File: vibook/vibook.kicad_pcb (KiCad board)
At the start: 2 copper layers, 15 x 89.5 mm, 53 parts, among them IC3 STLQ020C33R, J1 Conn_ARM_JTAG_SWD_10, SW3 SW_Push, U2 STM32L011K4Ux, U3 MPR121QR2, U5 MPR121QR2

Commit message: updated board design
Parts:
- removed U1, U4: ~, jlc:12matrix
- added C12: 470u, Capacitor_Tantalum_SMD:CP_EIA-7360-38_Kemet-E, F.Cu at (102.6, 111.5)
- added J2: 6861XX148922_686112148922, 6861XX148922_686112148922:686112148922, F.Cu at (51.0, 107.5)
- added J3: 6861XX148922_686112148922, 6861XX148922_686112148922:686112148922, F.Cu at (31.5, 107.5)
- U6: value ~ -> DFR0299; footprint jlc:2pin -> DFR0299:MODULE_DFR0299
- U7: footprint jlc:2pin -> Connector_Molex:Molex_PicoBlade_53047-0210_1x02_P1.25mm_Vertical
- U9: footprint jlc:2pin -> Connector_PinHeader_2.54mm:PinHeader_1x02_P2.54mm_Horizontal
- moved R2 112.7 mm to (25.0, 96.8), turned to -90 degrees
- moved C11 111.5 mm to (27.5, 95.3), turned to 180 degrees
- moved R19 109.3 mm to (23.5, 101.5), turned to -90 degrees
- moved R20 107.7 mm to (25.0, 101.5), turned to -90 degrees
- moved R21 106.0 mm to (26.5, 101.5), turned to -90 degrees
- moved U5 104.7 mm to (31.2, 97.5), turned to -90 degrees
- moved R22 104.4 mm to (28.0, 101.5), turned to -90 degrees
- moved R23 102.8 mm to (29.5, 101.5), turned to -90 degrees
- moved C7 102.0 mm to (35.5, 96.5), turned to 180 degrees
- moved R24 101.2 mm to (31.0, 101.5), turned to -90 degrees
- moved R25 99.6 mm to (32.5, 101.5), turned to -90 degrees
- moved R26 98.0 mm to (34.0, 101.5), turned to -90 degrees
- moved R27 96.5 mm to (35.5, 101.5), turned to -90 degrees
- moved R3 95.1 mm to (43.8, 98.0), turned to 0 degrees
- moved R28 95.0 mm to (37.0, 101.5), turned to -90 degrees
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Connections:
- C6 pad 2: Net-(IC3-EN) -> +4.5V
- IC3 pad 1: Net-(IC3-EN) -> +4.5V
- IC3 pad 3: Net-(IC3-EN) -> +4.5V
- R31 pad 1: Net-(U6-P1) -> Net-(U6-TX)
- U6 pad 1: Net-(U6-P1) -> +4.5V
- U7 pad 1: Net-(IC3-EN) -> Net-(U6-SPK1)
- U7 pad 2: GND -> Net-(U6-SPK2)
- U9 pad 1: Net-(IC3-EN) -> +4.5V
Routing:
- net +4.5V: track 0.00 -> 93.5 mm, vias 0 -> 2
- net Net-(U6-TX): track 0.00 -> 45.2 mm, vias 0 -> 4
- net Net-(IC3-EN): track 21.7 -> 0.00 mm
- net Net-(U6-SPK1): track 0.00 -> 20.4 mm
- net Net-(U2-PA3): track 30.5 -> 49.9 mm, vias 0 -> 4
- net Net-(U6-SPK2): track 0.00 -> 15.7 mm
- net GND: track 44.8 -> 33.3 mm, vias 23 -> 32
- net Net-(U2-PA4): track 72.5 -> 61.7 mm, vias 3 -> 2
- net Net-(U6-P1): track 6.17 -> 0.00 mm
- net +3.3V: track 133.2 -> 128.4 mm
- net Net-(J1-SWDIO/TMS): track 36.0 -> 32.8 mm
- net Net-(U2-PA5): track 64.8 -> 61.8 mm
- net Net-(U2-PA10): track 60.2 -> 57.3 mm, vias 2 -> 4
- net Net-(J1-~{RESET}): track 63.1 -> 65.8 mm
- net Net-(U3-REXT): track 3.20 -> 5.64 mm
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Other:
- board size 15 x 89.5 mm -> 123.5 x 21.3 mm
- board text removed: "Rx"
- board text removed: "Tx"

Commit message: updated schematic
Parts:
- moved R31 0.36 mm to (83.0, 102.5), turned to 0 degrees
- turned R4 to -90 degrees
- turned R5 to -90 degrees
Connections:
- net Net-(J1-SWCLK/TCK) renamed /SYS_SWCLK
- net Net-(J1-SWDIO/TMS) renamed /SYS_SWDIO
- net Net-(J1-~{RESET}) renamed /NRST
- net Net-(J2-Pad1) renamed /ELE0_0
- net Net-(J2-Pad10) renamed /ELE0_9
- net Net-(J2-Pad11) renamed /ELE0_10
- net Net-(J2-Pad12) renamed /ELE0_11
- net Net-(J2-Pad2) renamed /ELE0_1
- net Net-(J2-Pad3) renamed /ELE0_2
- net Net-(J2-Pad4) renamed /ELE0_3
- net Net-(J2-Pad5) renamed /ELE0_4
- net Net-(J2-Pad6) renamed /ELE0_5
- net Net-(J2-Pad7) renamed /ELE0_6
- net Net-(J2-Pad8) renamed /ELE0_7
- net Net-(J2-Pad9) renamed /ELE0_8
- net Net-(J3-Pad1) renamed /ELE1_0
- net Net-(J3-Pad10) renamed /ELE1_9
- net Net-(J3-Pad11) renamed /ELE1_10
- net Net-(J3-Pad12) renamed /ELE1_11
- net Net-(J3-Pad2) renamed /ELE1_1
- net Net-(J3-Pad3) renamed /ELE1_2
- net Net-(J3-Pad4) renamed /ELE1_3
- net Net-(J3-Pad5) renamed /ELE1_4
- net Net-(J3-Pad6) renamed /ELE1_5
- net Net-(J3-Pad7) renamed /ELE1_6
- net Net-(J3-Pad8) renamed /ELE1_7
- net Net-(J3-Pad9) renamed /ELE1_8
- R31 pad 1: Net-(U6-TX) -> /USART2_TX
- R31 pad 2: Net-(U2-PA2) -> Net-(U6-RX)
- R4 pad 1: +3.3V -> /I2C1_SDA
- R4 pad 2: Net-(U2-PA10) -> +3.3V
- R5 pad 1: +3.3V -> /I2C1_SCL
- R5 pad 2: Net-(U2-PA4) -> +3.3V
- R6 pad 2: Net-(U2-PA5) -> /EXTI5
- U2 pad 10: Net-(U2-PA4) -> /I2C1_SCL
- U2 pad 11: Net-(U2-PA5) -> /EXTI5
- U2 pad 12: unconnected-(U2-PA6-Pad12) -> /EXTI6
- U2 pad 20: Net-(U2-PA10) -> /I2C1_SDA
- U2 pad 8: Net-(U2-PA2) -> /USART2_TX
- U2 pad 9: Net-(U2-PA3) -> /USART2_RX
- U3 pad 1: Net-(U2-PA5) -> /EXTI5
- U3 pad 2: Net-(U2-PA4) -> /I2C1_SCL
- U3 pad 3: Net-(U2-PA10) -> /I2C1_SDA
- U5 pad 1: Net-(U2-PA5) -> /EXTI6
- U5 pad 2: Net-(U2-PA4) -> /I2C1_SCL
- U5 pad 3: Net-(U2-PA10) -> /I2C1_SDA
- U5 pad 4: Net-(U2-PA10) -> /I2C1_SDA
- U6 pad 2: Net-(U2-PA3) -> Net-(U6-RX)
- U6 pad 3: Net-(U6-TX) -> /USART2_RX
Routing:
- net Net-(U2-PA5): track 61.8 -> 0.00 mm, vias 4 -> 0
- net Net-(U2-PA4): track 61.7 -> 0.00 mm, vias 2 -> 0
- net /I2C1_SCL: track 0.00 -> 61.7 mm, vias 0 -> 2
- net Net-(U2-PA10): track 57.3 -> 0.00 mm, vias 4 -> 0
- net /I2C1_SDA: track 0.00 -> 57.3 mm, vias 0 -> 4
- net /EXTI6: track 0.00 -> 57.2 mm, vias 0 -> 4
- net /USART2_RX: track 0.00 -> 53.2 mm, vias 0 -> 4
- net Net-(U2-PA3): track 49.9 -> 0.00 mm, vias 4 -> 0
- net /EXTI5: track 0.00 -> 47.7 mm, vias 0 -> 4
- net Net-(U6-TX): track 45.2 -> 0.00 mm, vias 4 -> 0
- net Net-(U6-RX): track 0.00 -> 43.8 mm, vias 0 -> 4
- net Net-(U2-PA2): track 7.54 -> 0.00 mm, vias 2 -> 0
- net /USART2_TX: track 0.00 -> 7.38 mm, vias 0 -> 2

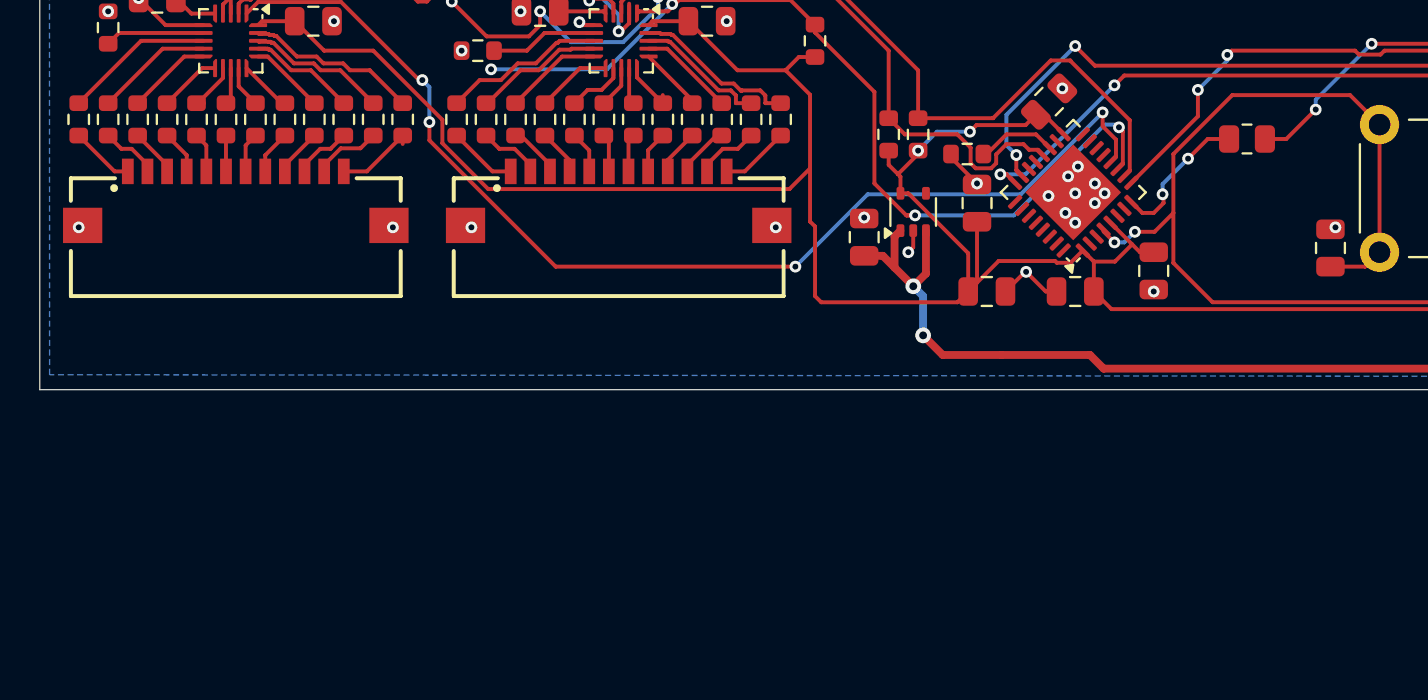
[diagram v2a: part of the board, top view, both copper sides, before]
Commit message: changed ffc connectors and added different mcu
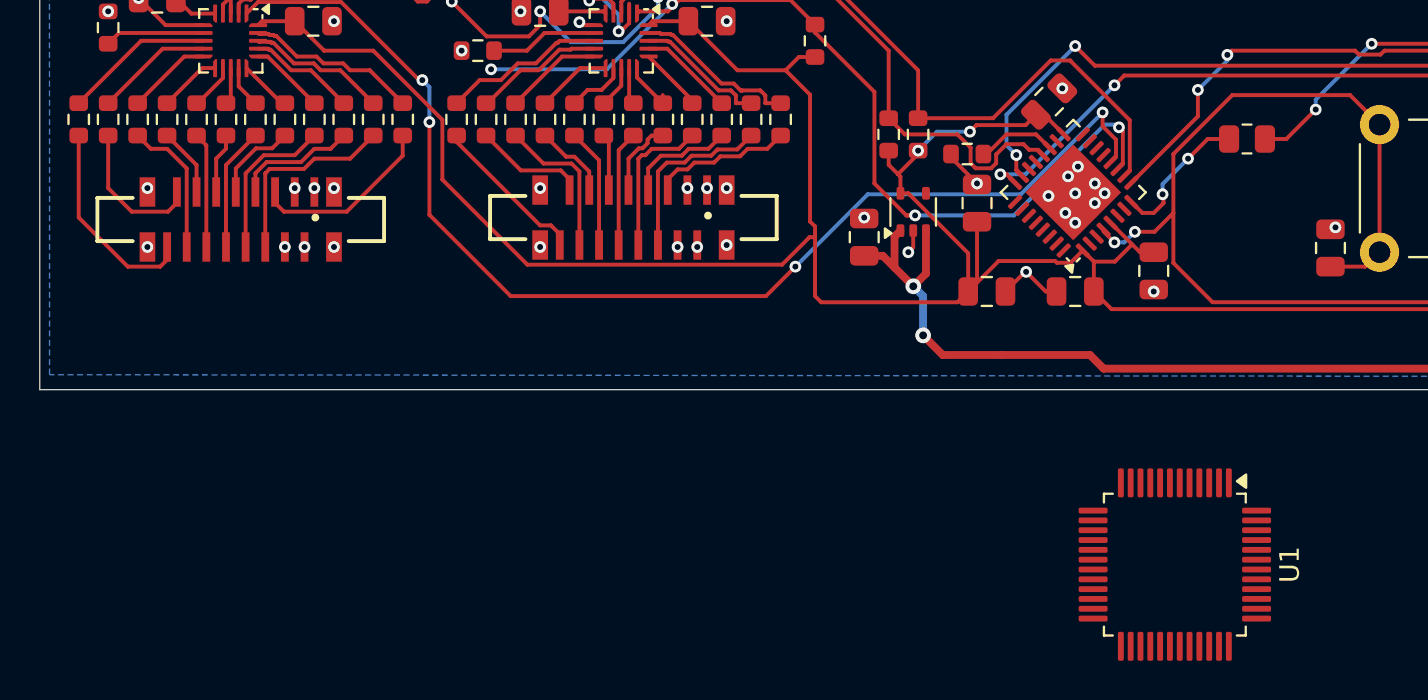
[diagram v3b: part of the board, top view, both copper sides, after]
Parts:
- removed J2, J3: 6861XX148922_686112148922, 6861XX148922_686112148922:686112148922
- added J4: 6873XX124422_687316124422, 687316124422:687316124422, F.Cu at (51.8, 106.5)
- added J5: 6873XX124422_687316124422, 687316124422:687316124422, F.Cu at (31.8, 106.6)
- added U1: STM32L072CBTx, Package_QFP:LQFP-48_7x7mm_P0.5mm, F.Cu at (79.3, 124.2)
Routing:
- net /ELE1_0: track 3.26 -> 10.5 mm
- net /ELE1_10: track 3.45 -> 10.0 mm
- net /ELE0_10: track 3.21 -> 9.25 mm
- net /ELE1_8: track 2.45 -> 8.05 mm
- net /ELE0_2: track 2.72 -> 8.04 mm
- net /ELE0_8: track 2.34 -> 7.63 mm
- net /ELE1_11: track 4.19 -> 9.44 mm
- net /ELE1_2: track 2.45 -> 7.19 mm
- net /ELE0_0: track 3.51 -> 8.07 mm
- net /ELE1_1: track 2.96 -> 7.41 mm
- net /ELE1_6: track 2.03 -> 6.30 mm
- net /ELE0_6: track 1.93 -> 5.88 mm
- net /ELE0_4: track 2.14 -> 6.09 mm
- net /ELE1_4: track 2.03 -> 5.88 mm
- net /ELE0_11: track 3.50 -> 7.22 mm
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
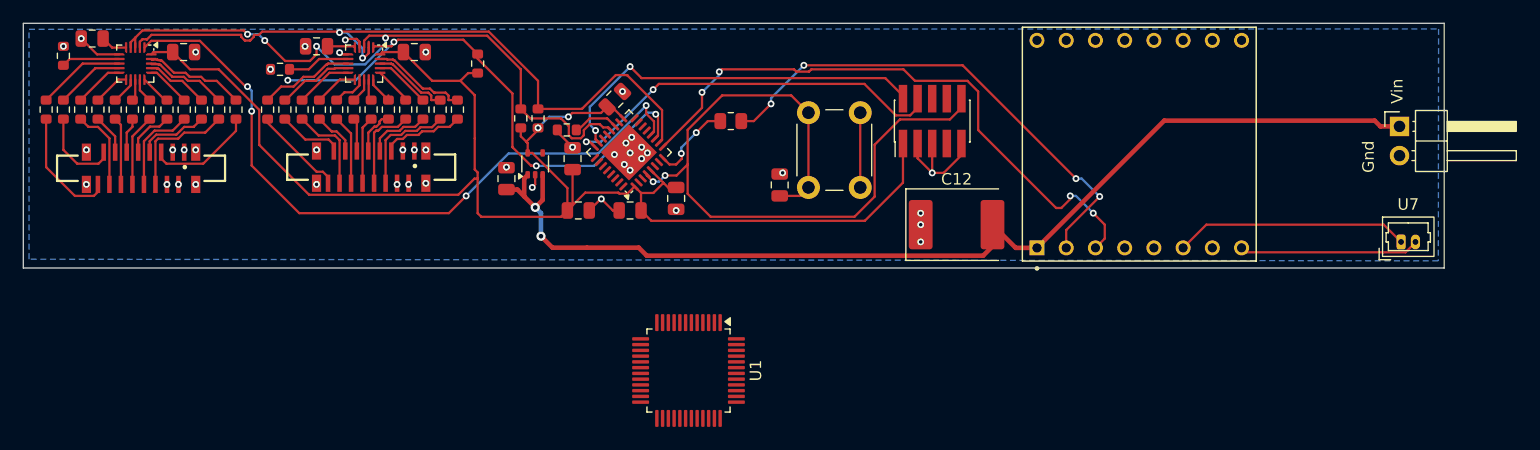
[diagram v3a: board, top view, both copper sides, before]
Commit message: started mcu upgrade and rerouting
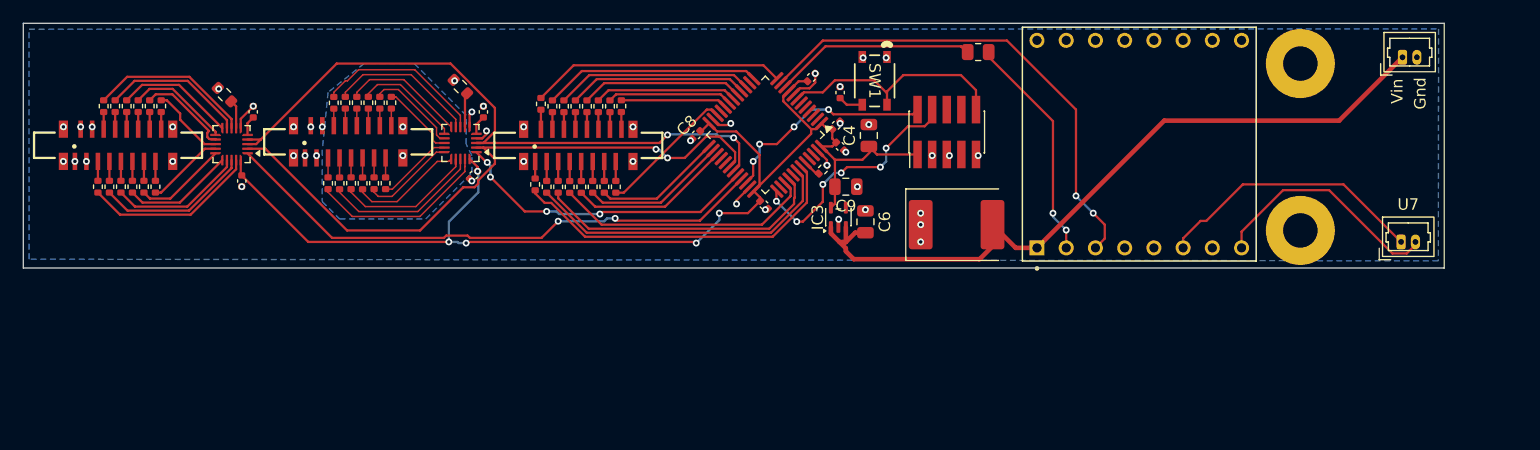
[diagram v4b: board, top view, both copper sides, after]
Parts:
- removed R1, R6: 10k, Resistor_SMD:R_0603_1608Metric
- removed R4, R5: 4.7k, Resistor_SMD:R_0603_1608Metric
- removed SW3: SW_Push, Button_Switch_THT:SW_PUSH_6mm_H4.3mm
- removed U2: STM32L011K4Ux, Package_DFN_QFN:QFN-32-1EP_5x5mm_P0.5mm_EP3.45x3.45mm
- added C13: 1u, Capacitor_SMD:C_0402_1005Metric, F.Cu at (92.5, 104.7)
- added C14: 1u, Capacitor_SMD:C_0402_1005Metric, F.Cu at (40.5, 107.7)
- added J6: 6873XX124422_687316124422, 687316124422:687316124422, F.Cu at (69.8, 104.6)
- added R32: 10k, Resistor_SMD:R_0402_1005Metric, F.Cu at (91.0, 106.7)
- added R33: 10k, Resistor_SMD:R_0402_1005Metric, F.Cu at (73.5, 101.2)
- added R34: 10k, Resistor_SMD:R_0402_1005Metric, F.Cu at (73.0, 108.2)
- added R35: 10k, Resistor_SMD:R_0402_1005Metric, F.Cu at (72.5, 101.2)
- added R36: 10k, Resistor_SMD:R_0402_1005Metric, F.Cu at (72.0, 108.2)
- added R37: 10k, Resistor_SMD:R_0402_1005Metric, F.Cu at (71.5, 101.2)
- added R38: 10k, Resistor_SMD:R_0402_1005Metric, F.Cu at (71.0, 108.2)
- added R39: 10k, Resistor_SMD:R_0402_1005Metric, F.Cu at (70.5, 101.2)
- added R40: 10k, Resistor_SMD:R_0402_1005Metric, F.Cu at (70.0, 108.2)
- added R41: 10k, Resistor_SMD:R_0402_1005Metric, F.Cu at (69.5, 101.2)
- added R42: 10k, Resistor_SMD:R_0402_1005Metric, F.Cu at (69.0, 108.2)
- added R43: 10k, Resistor_SMD:R_0402_1005Metric, F.Cu at (68.5, 101.2)
- added R44: 10k, Resistor_SMD:R_0402_1005Metric, F.Cu at (68.0, 108.2)
- added R45: 10k, Resistor_SMD:R_0402_1005Metric, F.Cu at (67.5, 101.2)
- added R46: 10k, Resistor_SMD:R_0402_1005Metric, F.Cu at (67.0, 108.2)
- added R47: 10k, Resistor_SMD:R_0402_1005Metric, F.Cu at (66.5, 101.0)
- added R48: 10k, Resistor_SMD:R_0402_1005Metric, F.Cu at (66.0, 108.0)
- added REF**: MountingHole_3mm_Pad, MountingHole:MountingHole_3mm_Pad, F.Cu at (132.5, 112.0)
- added REF**: MountingHole_3mm_Pad, MountingHole:MountingHole_3mm_Pad, F.Cu at (132.5, 97.5)
- added SW1: SKRPADE010, footprints:SKRPADE010_AAL, F.Cu at (95.5, 99.0)
- C1, C2, C3, C7, C8: value 100n -> 1u; footprint Capacitor_SMD:C_0805_2012Metric -> Capacitor_SMD:C_0402_1005Metric
- C10, C11, C5: footprint Capacitor_SMD:C_0805_2012Metric -> Capacitor_SMD:C_0402_1005Metric
- R10, R11, R12, R13, R14, R15, R16, R17, R18, R19, R20, R21, R22, R23, R24, R25, R26, R27, R28, R29, R30, R7, R8, R9: footprint Resistor_SMD:R_0603_1608Metric -> Resistor_SMD:R_0402_1005Metric
- U9: footprint Connector_PinHeader_2.54mm:PinHeader_1x02_P2.54mm_Horizontal -> Connector_Molex:Molex_PicoBlade_53047-0210_1x02_P1.25mm_Vertical
- moved C6 31.4 mm to (94.7, 111.2)
- moved C7 27.4 mm to (60.7, 107.2), turned to 45 degrees
- moved IC3 26.8 mm to (92.3, 110.9)
- moved C4 25.8 mm to (95.0, 103.8)
- moved C8 25.5 mm to (80.0, 103.7), turned to 45 degrees
- moved C9 23.3 mm to (93.0, 108.2)
- moved R31 22.3 mm to (104.5, 96.5)
- moved U1 21.5 mm to (86.0, 103.7), turned to -135 degrees
- moved C3 17.2 mm to (90.0, 98.7)
- moved R3 15.7 mm to (59.5, 99.5), turned to -45 degrees
- moved C10 15.6 mm to (61.5, 101.7), turned to 90 degrees
- moved C11 15.4 mm to (41.5, 101.7), turned to 90 degrees
- moved C2 15.3 mm to (92.2, 102.9), turned to 45 degrees
- moved R2 14.4 mm to (39.0, 100.2), turned to -45 degrees
- moved R30 13.7 mm to (28.0, 108.2), turned to 90 degrees
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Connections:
- C5 pad 1: /NRST -> Net-(C5-Pad1)
- J4 pad 10: /ELE0_6 -> /ELE0_2
- J4 pad 11: /ELE0_5 -> /ELE0_8
- J4 pad 12: /ELE0_4 -> /ELE0_3
- J4 pad 13: /ELE0_3 -> /ELE0_7
- J4 pad 14: /ELE0_2 -> /ELE0_4
- J4 pad 15: /ELE0_1 -> /ELE0_6
- J4 pad 16: /ELE0_0 -> /ELE0_5
- J4 pad 6: /ELE0_10 -> /ELE0_0
- J4 pad 7: /ELE0_9 -> /ELE0_10
- J4 pad 8: /ELE0_8 -> /ELE0_1
- J4 pad 9: /ELE0_7 -> /ELE0_9
- J5 pad 10: /ELE1_6 -> /ELE1_2
- J5 pad 11: /ELE1_5 -> /ELE1_8
- J5 pad 12: /ELE1_4 -> /ELE1_3
- J5 pad 13: /ELE1_3 -> /ELE1_7
- J5 pad 14: /ELE1_2 -> /ELE1_4
- J5 pad 15: /ELE1_1 -> /ELE1_6
- J5 pad 16: /ELE1_0 -> /ELE1_5
- J5 pad 6: /ELE1_10 -> /ELE1_0
- J5 pad 7: /ELE1_9 -> /ELE1_10
- J5 pad 8: /ELE1_8 -> /ELE1_1
- J5 pad 9: /ELE1_7 -> /ELE1_9
- R31 pad 1: /USART2_TX -> /USART4_TX
- U1 pad 1: unconnected-(U1-VDD-Pad1) -> +3.3V
- U1 pad 10: unconnected-(U1-PA0-Pad10) -> /USART4_TX
- U1 pad 11: unconnected-(U1-PA1-Pad11) -> /USART4_RX
- U1 pad 12: unconnected-(U1-PA2-Pad12) -> /TSC0
- U1 pad 13: unconnected-(U1-PA3-Pad13) -> /TSC1
- U1 pad 15: unconnected-(U1-PA5-Pad15) -> /TSC2
- U1 pad 16: unconnected-(U1-PA6-Pad16) -> /TSC3
- U1 pad 17: unconnected-(U1-PA7-Pad17) -> /TSC4
- U1 pad 18: unconnected-(U1-PB0-Pad18) -> /TSC5
- U1 pad 19: unconnected-(U1-PB1-Pad19) -> /TSC6
- U1 pad 20: unconnected-(U1-PB2-Pad20) -> /TSC7
- U1 pad 22: unconnected-(U1-PB11-Pad22) -> /TSC12
- U1 pad 23: Net-(U1-VSS-Pad23) -> GND
- U1 pad 24: unconnected-(U1-VDD-Pad24) -> +3.3V
- U1 pad 25: unconnected-(U1-PB12-Pad25) -> /TSC13
- U1 pad 26: unconnected-(U1-PB13-Pad26) -> /TSC14
- U1 pad 27: unconnected-(U1-PB14-Pad27) -> /TSC15
- U1 pad 30: unconnected-(U1-PA9-Pad30) -> /I2C1_SCL
- U1 pad 31: unconnected-(U1-PA10-Pad31) -> /I2C1_SDA
- U1 pad 32: unconnected-(U1-PA11-Pad32) -> /EXTI11
- U1 pad 33: unconnected-(U1-PA12-Pad33) -> /EXTI12
- U1 pad 34: unconnected-(U1-PA13-Pad34) -> /SYS_SWDIO
- U1 pad 35: Net-(U1-VSS-Pad23) -> GND
- U1 pad 36: unconnected-(U1-VDD_USB-Pad36) -> +3.3V
- U1 pad 37: unconnected-(U1-PA14-Pad37) -> /SYS_SWCLK
- U1 pad 39: unconnected-(U1-PB3-Pad39) -> /TSC8
- U1 pad 40: unconnected-(U1-PB4-Pad40) -> /TSC9
- U1 pad 42: unconnected-(U1-PB6-Pad42) -> /TSC10
- U1 pad 43: unconnected-(U1-PB7-Pad43) -> /TSC11
- U1 pad 44: unconnected-(U1-BOOT0-Pad44) -> Net-(U1-BOOT0)
- U1 pad 47: Net-(U1-VSS-Pad23) -> GND
- U1 pad 48: unconnected-(U1-VDD-Pad48) -> +3.3V
- U1 pad 7: unconnected-(U1-NRST-Pad7) -> /NRST
- U1 pad 8: unconnected-(U1-VSSA-Pad8) -> GND
- U1 pad 9: unconnected-(U1-VDDA-Pad9) -> +3.3V
- U3 pad 1: /EXTI5 -> /EXTI11
- U5 pad 1: /EXTI6 -> /EXTI12
- U6 pad 3: /USART2_RX -> /USART4_RX
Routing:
- net /EXTI6: track 60.7 -> 0.00 mm, vias 4 -> 0
- net /USART2_RX: track 53.2 -> 0.00 mm, vias 4 -> 0
- net /EXTI12: track 0.00 -> 48.4 mm, vias 0 -> 2
- net /EXTI5: track 47.7 -> 0.00 mm, vias 4 -> 0
- net /NRST: track 65.8 -> 20.6 mm, vias 2 -> 0
- net /USART4_RX: track 0.00 -> 43.0 mm, vias 0 -> 2
- net /TSC11: track 0.00 -> 30.0 mm
- net +4.5V: track 93.5 -> 64.6 mm, vias 2 -> 0
- net +3.3V: track 131.5 -> 103.1 mm, vias 2 -> 5
- net /TSC10: track 0.00 -> 27.7 mm
- net /EXTI11: track 0.00 -> 26.9 mm, vias 0 -> 4
- net /TSC9: track 0.00 -> 25.4 mm
- net Net-(U6-RX): track 43.8 -> 19.8 mm, vias 4 -> 2
- net /TSC8: track 0.00 -> 22.7 mm
- net /TSC0: track 0.00 -> 22.2 mm
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
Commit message: finished spine pcb final design, sent for manufacture
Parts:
- removed the REF** at (132.5, 112.0)
- removed the REF** at (132.5, 97.5)
- added C15: 47n, Capacitor_SMD:C_0402_1005Metric, F.Cu at (89.0, 98.0)
- added C16: 47n, Capacitor_SMD:C_0402_1005Metric, F.Cu at (82.0, 97.0)
- added C17: 47n, Capacitor_SMD:C_0402_1005Metric, F.Cu at (81.0, 99.4)
- added C18: 47n, Capacitor_SMD:C_0402_1005Metric, F.Cu at (81.5, 107.9)
- added C19: 47n, Capacitor_SMD:C_0402_1005Metric, F.Cu at (89.6, 108.2)
- added C20: 47n, Capacitor_SMD:C_0402_1005Metric, F.Cu at (79.5, 101.4)
- added REF**: MountingHole_3mm, MountingHole:MountingHole_3mm, F.Cu at (132.5, 111.6)
- added REF**: MountingHole_3mm, MountingHole:MountingHole_3mm, F.Cu at (132.5, 97.6)
- moved C2 0.85 mm to (93.0, 103.0)
- moved C8 0.20 mm to (80.0, 103.5)
- moved C1 0.12 mm to (85.8, 109.7)
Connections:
- net /TSC6 renamed /TSC_G3_3
- net /TSC7 renamed /TSC_G3_4
- R31 pad 1: /USART4_TX -> /LPUART1_TX
- R34 pad 2: /TSC12 -> /TSC_G6_2
- R36 pad 2: /TSC13 -> /TSC_G6_3
- R37 pad 2: /TSC5 -> /TSC_G2_4
- R38 pad 2: /TSC14 -> /TSC_G6_4
- R39 pad 2: /TSC4 -> /TSC_G2_3
- R40 pad 2: /TSC15 -> /TSC_G4_2
- R41 pad 2: /TSC3 -> /TSC_G2_2
- R42 pad 2: /TSC8 -> /TSC_G4_3
- R43 pad 2: /TSC2 -> /TSC_G1_4
- R44 pad 2: /TSC9 -> /TSC_G4_4
- R45 pad 2: /TSC1 -> /TSC_G1_3
- R46 pad 2: /TSC10 -> /TSC_G5_1
- R47 pad 2: /TSC0 -> /TSC_G1_2
- R48 pad 2: /TSC11 -> /TSC_G5_2
- U1 pad 10: /USART4_TX -> /TSC_G1_1
- U1 pad 11: /USART4_RX -> /TSC_G1_2
- U1 pad 12: /TSC0 -> /TSC_G1_3
- U1 pad 13: /TSC1 -> /TSC_G1_4
- U1 pad 14: unconnected-(U1-PA4-Pad14) -> /TSC_G2_1
- U1 pad 15: /TSC2 -> /TSC_G2_2
- U1 pad 16: /TSC3 -> /TSC_G2_3
- U1 pad 17: /TSC4 -> /TSC_G2_4
- U1 pad 18: /TSC5 -> /TSC_G3_2
- U1 pad 21: unconnected-(U1-PB10-Pad21) -> /LPUART1_TX
- U1 pad 22: /TSC12 -> /TSC_G6_1
- U1 pad 25: /TSC13 -> /TSC_G6_2
- U1 pad 26: /TSC14 -> /TSC_G6_3
- U1 pad 27: /TSC15 -> /TSC_G6_4
- U1 pad 28: unconnected-(U1-PB15-Pad28) -> /EXTI12
- U1 pad 30: /I2C1_SCL -> /TSC_G4_1
- U1 pad 31: /I2C1_SDA -> /TSC_G4_2
- U1 pad 32: /EXTI11 -> /TSC_G4_3
- U1 pad 33: /EXTI12 -> /TSC_G4_4
- U1 pad 39: /TSC8 -> /TSC_G5_1
- U1 pad 40: /TSC9 -> /TSC_G5_2
- U1 pad 41: unconnected-(U1-PB5-Pad41) -> /EXTI11
- U1 pad 42: /TSC10 -> /TSC_G5_3
- U1 pad 43: /TSC11 -> unconnected-(U1-PB7-Pad43)
- U1 pad 45: unconnected-(U1-PB8-Pad45) -> /I2C1_SCL
- U1 pad 46: unconnected-(U1-PB9-Pad46) -> /I2C1_SDA
- U6 pad 3: /USART4_RX -> unconnected-(U6-TX-Pad3)
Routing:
- net /USART4_RX: track 43.0 -> 0.00 mm, vias 2 -> 0
- net /TSC11: track 30.0 -> 0.00 mm
- net /TSC10: track 27.7 -> 0.00 mm
- net /TSC_G5_2: track 0.00 -> 26.5 mm
- net /TSC_G1_2: track 0.00 -> 26.1 mm
- net /TSC9: track 25.4 -> 0.00 mm
- net /LPUART1_TX: track 0.00 -> 25.0 mm, vias 0 -> 2
- net /TSC_G5_1: track 0.00 -> 24.2 mm
- net /TSC_G1_3: track 0.00 -> 23.0 mm
- net /TSC8: track 22.7 -> 0.00 mm
- net /TSC0: track 22.2 -> 0.00 mm
- net /TSC_G1_4: track 0.00 -> 20.1 mm
- net /TSC1: track 18.8 -> 0.00 mm
- net /I2C1_SCL: track 54.5 -> 73.1 mm, vias 2 -> 6
- net /I2C1_SDA: track 57.3 -> 75.9 mm
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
